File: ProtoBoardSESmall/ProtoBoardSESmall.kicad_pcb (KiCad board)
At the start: 2 copper layers, 38 x 43 mm, 35 parts, among them J1 TYPE-C-31-M-12, J10 BM05B-SRSS-TB_LF__SN_, J11 Conn_01x05_Female, J2 TYPE-C-31-M-12, J3 BM10B-SRSS-TB_LF__SN_, J4 Conn_01x05_Female, J5 BM05B-SRSS-TB_LF__SN_, J6 BM05B-SRSS-TB_LF__SN_, J7 Conn_01x05_Female, J8 BM05B-SRSS-TB_LF__SN_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

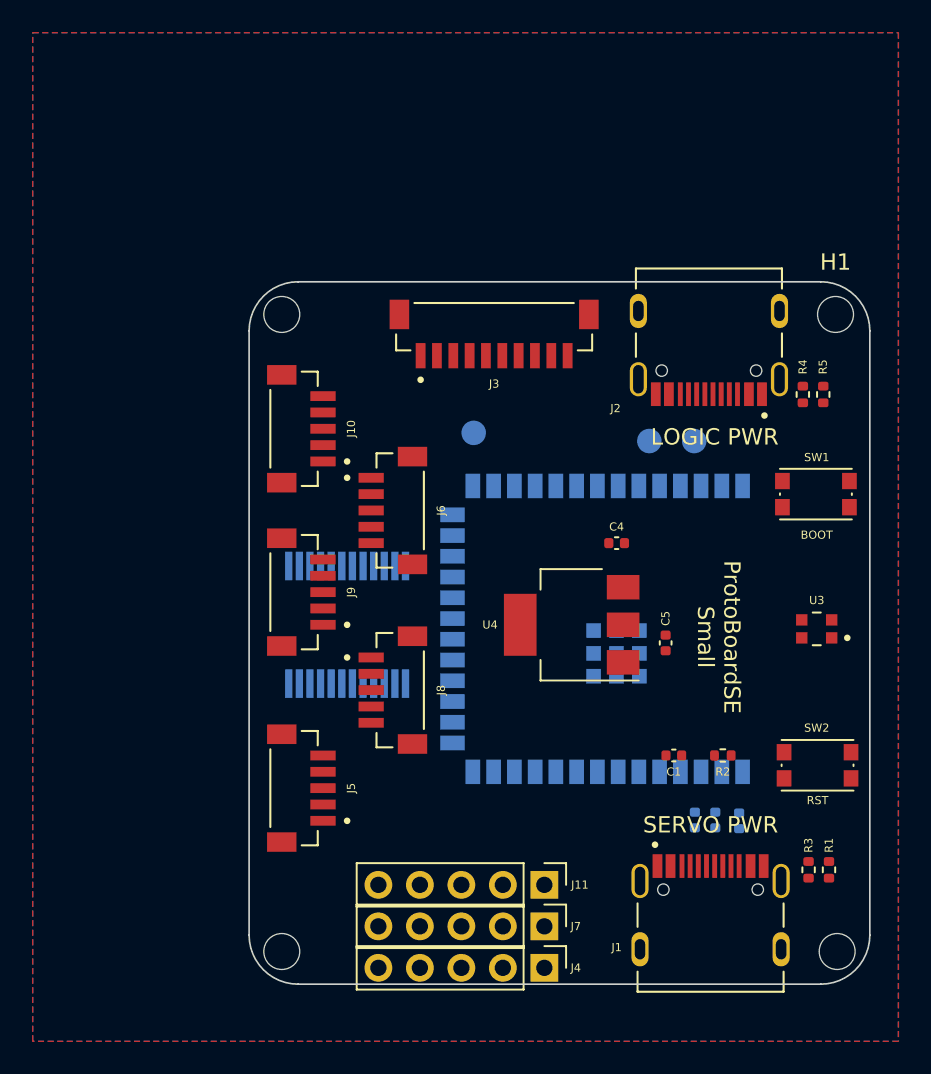
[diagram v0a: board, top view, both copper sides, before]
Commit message: Add lcsc references, routing wip
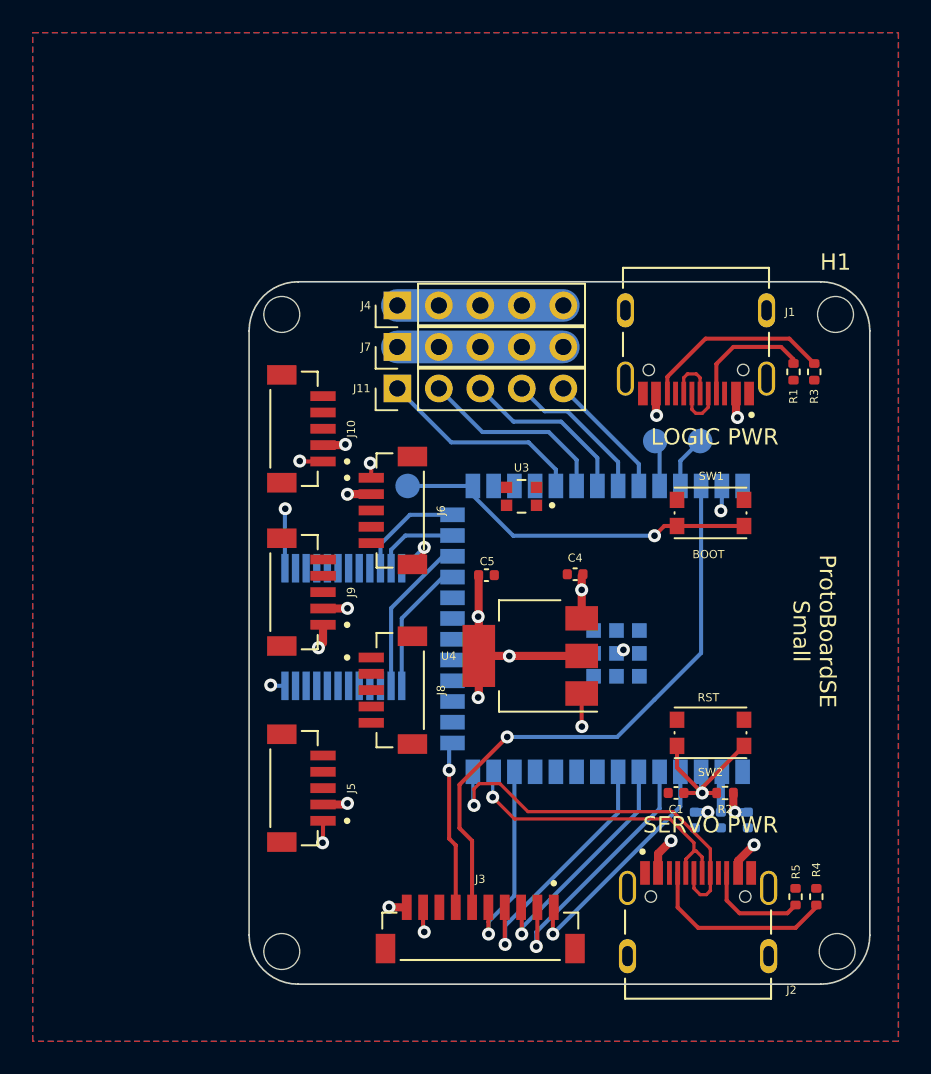
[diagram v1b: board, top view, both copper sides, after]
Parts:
- moved J4 41.5 mm to (179.1, 44.5), turned to 90 degrees
- moved J2 39.5 mm to (197.5, 84.3), turned to 0 degrees
- moved J1 39.1 mm to (197.4, 44.7), turned to 180 degrees
- moved J3 38.8 mm to (184.2, 83.8), turned to 180 degrees
- moved J7 36.6 mm to (179.1, 47.0), turned to 90 degrees
- moved J11 31.7 mm to (179.1, 49.5), turned to 90 degrees
- moved R5 30.8 mm to (203.5, 80.6), turned to 90 degrees
- moved R4 30.8 mm to (204.7, 80.6), turned to -90 degrees
- moved R1 30.6 mm to (203.3, 48.5), turned to 90 degrees
- moved R3 30.5 mm to (204.6, 48.5), turned to -90 degrees
- moved U3 19.8 mm to (186.7, 56.1)
- moved C5 11.7 mm to (184.5, 61.0), turned to 0 degrees
- moved SW2 6.85 mm to (198.2, 70.6)
- moved SW1 6.55 mm to (198.2, 57.1)
- moved TP4 5.19 mm to (179.7, 55.5)
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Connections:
- J11 pad 1: /Servo1 -> /Servo5
- J11 pad 2: /Servo2 -> /Servo4
- J11 pad 4: /Servo4 -> /Servo2
- J11 pad 5: /Servo5 -> /Servo1
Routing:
- net +3V3: track 0.00 -> 46.9 mm, vias 0 -> 11
- net /JoyX: track 0.00 -> 36.2 mm, vias 0 -> 1
- net /COM1: track 0.00 -> 32.3 mm, vias 0 -> 2
- net /USB1_DP: track 0.00 -> 24.1 mm, vias 0 -> 1
- net /BOOT0: track 0.00 -> 22.4 mm, vias 0 -> 1
- net GND: track 0.00 -> 22.3 mm, vias 0 -> 8
- net /USB1_DN: track 0.00 -> 18.7 mm, vias 0 -> 1
- net /ButC: track 0.00 -> 16.2 mm, vias 0 -> 1
- net /Menu: track 0.00 -> 15.7 mm, vias 0 -> 1
- net /ButJ: track 0.00 -> 14.8 mm, vias 0 -> 1
- net /ButB: track 0.00 -> 14.6 mm, vias 0 -> 1
- net /VBUS0: track 0.00 -> 13.0 mm, vias 0 -> 2
- net /Servo5: track 0.00 -> 12.8 mm
- net /ButA: track 0.00 -> 12.2 mm, vias 0 -> 1
- net /Servo4: track 0.00 -> 11.8 mm
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- added copper zone on In2.Cu, net +3V3
- added copper zone on In1.Cu, net /VBUS0
- added copper zone on In1.Cu, net /VBUS1
- added copper zone on In1.Cu, net GND
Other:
- copper layers 2 -> 4

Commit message: Routing done + production files
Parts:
- added C7: 0.1uF, Capacitor_SMD:C_0402_1005Metric, F.Cu at (186.6, 58.4)
- added TP1: TestPoint, TestPoint:TestPoint_Pad_D1.5mm, B.Cu at (195.6, 44.6)
- added TP5: TestPoint, TestPoint:TestPoint_Pad_D1.5mm, B.Cu at (198.8, 44.6)
- added TP6: TestPoint, TestPoint:TestPoint_Pad_D1.5mm, B.Cu at (195.5, 84.5)
- added TP7: TestPoint, TestPoint:TestPoint_Pad_D1.5mm, B.Cu at (199.2, 84.5)
- added TP8: TestPoint, TestPoint:TestPoint_Pad_D1.5mm, B.Cu at (176.3, 84.2)
- added TP9: TestPoint, TestPoint:TestPoint_Pad_D1.5mm, B.Cu at (179.4, 84.2)
- C2, C3, C6: moved to F.Cu
- moved C2 3.37 mm to (200.6, 75.3)
- moved C6 3.24 mm to (197.4, 75.3)
- moved R2 1.19 mm to (199.6, 73.2)
- moved C1 1.12 mm to (195.9, 73.2)
- moved C3 0.64 mm to (199.0, 75.3)
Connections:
- J3 pad 8: /CH7 -> /CH15
- J5 pad 3: /CH10 -> /CH9
- J5 pad 4: /CH9 -> /CH10
- J5 pad 5: /CH8 -> /CH11
- J8 pad 3: /CH13 -> /CH14
- J8 pad 4: /CH12 -> /CH13
- J8 pad 5: /CH11 -> /CH12
- J9 pad 3: /CH14 -> /CH16
- J9 pad 4: /CH15 -> /CH8
- J9 pad 5: /CH16 -> /CH7
- U1 pad 30: unconnected-(U1-Pad30) -> /RGB
- U3 pad 2: unconnected-(U3-Pad2) -> GND
- U3 pad 3: unconnected-(U3-Pad3) -> /RGB
- U3 pad 4: unconnected-(U3-Pad4) -> +3V3
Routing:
- net /CH15: track 0.00 -> 15.7 mm, vias 0 -> 1
- net /CH6: track 0.00 -> 15.2 mm, vias 0 -> 1
- net /CH5: track 0.00 -> 13.6 mm, vias 0 -> 1
- net /CH4: track 0.00 -> 12.0 mm, vias 0 -> 1
- net /CH2: track 0.00 -> 9.04 mm, vias 0 -> 1
- net /CH9: track 0.00 -> 8.94 mm, vias 0 -> 1
- net /CH3: track 0.00 -> 8.34 mm, vias 0 -> 1
- net /CH16: track 0.00 -> 8.08 mm, vias 0 -> 1
- net /CH10: track 0.00 -> 6.99 mm, vias 0 -> 1
- net /CH12: track 0.00 -> 6.46 mm, vias 0 -> 1
- net /CH14: track 0.00 -> 5.80 mm, vias 0 -> 1
- net /CH7: track 0.00 -> 5.56 mm, vias 0 -> 1
- net /CH1: track 0.00 -> 5.53 mm, vias 0 -> 1
- net /RGB: track 0.00 -> 5.05 mm, vias 0 -> 1
- net /CH11: track 0.00 -> 4.79 mm, vias 0 -> 1
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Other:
- board text added: "3.3V"
- board text added: "5V Logic"
- board text added: "5V Servo"
- board text added: "GND"

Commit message: ProtoboardSmall : Add QWIIC connector + switch USB C label
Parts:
- added J12: Qwiic_Vertical, SparkFun-Connector:JST04_1MM_Vertical, F.Cu at (180.0, 76.2)
- added R6: 10K, Resistor_SMD:R_0402_1005Metric, F.Cu at (175.1, 80.5)
- added R7: 10K, Resistor_SMD:R_0402_1005Metric, F.Cu at (176.5, 80.5)
- moved TP4 1.61 mm to (179.9, 53.9)
- moved J8 1.60 mm to (180.0, 66.4)
- moved J6 0.90 mm to (180.0, 56.1)
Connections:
- U1 pad 17: unconnected-(U1-GPIO9/TOUCH9/ADC1_CH8/FSPIHD/SUBSPIHD-Pad17) -> /I2C_SCL
- U1 pad 18: unconnected-(U1-GPIO10/TOUCH10/ADC1_CH9/FSPICS0/FSPIIO4/SUBSPICS0-Pad18) -> /I2C_SDA
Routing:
- net /I2C_SDA: track 0.00 -> 17.6 mm, vias 0 -> 1
- net /I2C_SCL: track 0.00 -> 16.3 mm, vias 0 -> 1
- net +3V3: track 49.1 -> 56.4 mm, vias 14 -> 12
- net /CH15: track 15.7 -> 21.7 mm
- net /CH3: track 8.34 -> 3.34 mm
- net /CH2: track 9.04 -> 5.37 mm
- net GND: track 26.6 -> 24.7 mm, vias 22 -> 23
- net /CH12: track 6.46 -> 4.64 mm
- net /CH1: track 5.53 -> 7.05 mm
- net /CH14: track 5.80 -> 4.40 mm
- net /CH13: track 4.56 -> 5.85 mm
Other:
- board text added: "QWIIC"
